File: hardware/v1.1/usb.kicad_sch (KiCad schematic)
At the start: 27 parts, among them J3 USB_C_Receptacle_USB2.0_14P, J4 USB_C_Receptacle_USB2.0_14P, J5 USB_C_Receptacle_USB2.0_14P, U1 ECP5U_12_CABGA256, U6 FT231XQ, U7 TPD2EUSB30A, U8 TPD2EUSB30A, U9 TPD2EUSB30A

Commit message: Improvements of v1.1
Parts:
- added R39, R40, R41, R42: 15k, Resistor_SMD:R_0402_1005Metric, symbol Device:R
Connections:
- net D2+: now also R39.2
- net D2-: now also R40.2
- net D3+: now also R41.2
- net D3-: now also R42.2
- new net USB2_PULL: R39.1, R40.1
- new net USB3_PULL: R41.1, R42.1

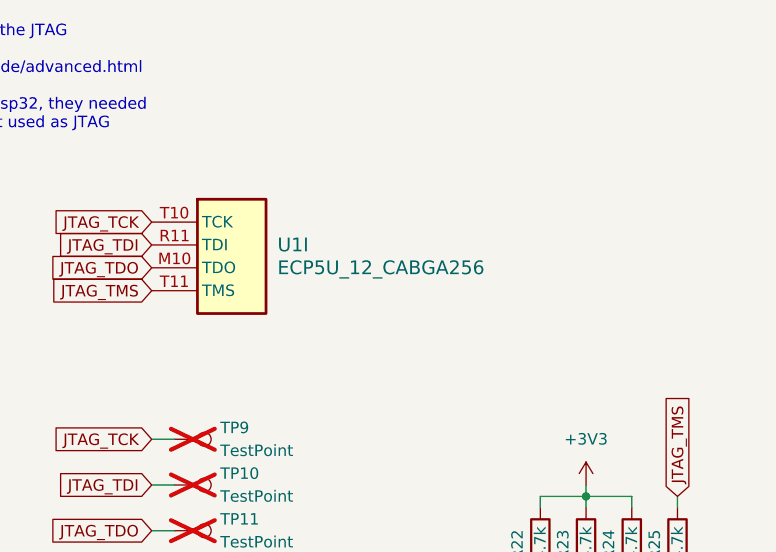
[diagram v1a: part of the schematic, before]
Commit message: Clean up the design by a bit
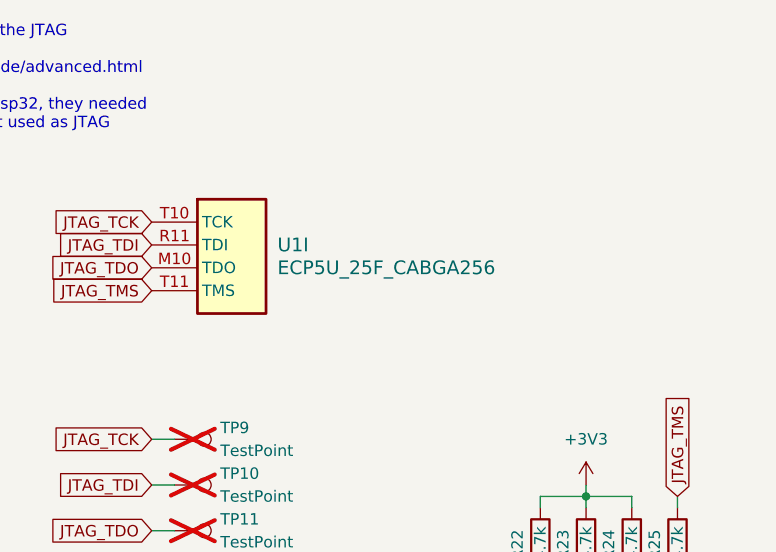
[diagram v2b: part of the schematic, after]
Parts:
- U1: value ECP5U_12_CABGA256 -> ECP5U_25F_CABGA256
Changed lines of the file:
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@@
 			)
 		)
-		(property "Value" "ECP5U_12_CABGA256"
+		(property "Value" "ECP5U_25F_CABGA256"
 			(at 195.58 52.0699 0)
 			(effects
